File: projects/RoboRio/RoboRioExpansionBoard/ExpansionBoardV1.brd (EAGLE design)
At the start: 100.3 x 80.3 mm, 83 parts, among them Q1 5MHz

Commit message: Deleted some capacitors
just for lol s♥♥♥♥♥♥♥♥
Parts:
- removed C1, C11, C6, C7, C8, C9: (no value), capacitor-wima:C7.5B6
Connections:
- net +3V3: no longer C1.1, C11.2, C6.1, C9.2
- net +5V: no longer C7.1, C8.1
- net GND: no longer C1.2, C11.1, C6.2, C7.2, C8.2, C9.1
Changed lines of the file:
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@@
 <element name="GREEN" library="led" package="LED5MM" value="" x="-91.44" y="-19.05"/>
 <element name="U$4" library="RESETBUTTON3000" package="RESETBUTTON300000MILLION" value="BUTTON" x="89.916" y="74.168" rot="R180"/>
-<element name="C1" library="capacitor-wima" package="C7.5B6" value="" x="-90.17" y="-27.432"/>
 <element name="C4" library="capacitor-wima" package="C7.5B6" value="" x="-90.17" y="-51.816"/>
 <element name="C5" library="capacitor-wima" package="C7.5B6" value="" x="-90.17" y="-59.944"/>
-<element name="C6" library="capacitor-wima" package="C7.5B6" value="" x="-90.17" y="-68.072"/>
-<element name="C7" library="capacitor-wima" package="C7.5B6" value="" x="-90.17" y="-76.2"/>
 <element name="C2" library="capacitor-wima" package="C7.5B6" value="" x="-90.17" y="-84.328"/>
-<element name="C8" library="capacitor-wima" package="C7.5B6" value="" x="-90.17" y="-100.584"/>
 <element name="C3" library="capacitor-wima" package="C7.5B6" value="" x="-90.17" y="-108.712"/>
-<element name="C9" library="capacitor-wima" package="C7.5B6" value="" x="-90.17" y="-116.84"/>
 <element name="C10" library="capacitor-wima" package="C7.5B6" value="" x="-90.17" y="-124.968"/>
-<element name="C11" library="capacitor-wima" package="C7.5B6" value="" x="-90.17" y="-133.096"/>
 <element name="C12" library="capacitor-wima" package="C7.5B6" value="" x="-90.17" y="-141.224"/>
 <element name="C13" library="capacitor-wima" package="C7.5B6" value="" x="-90.17" y="-149.352"/>
@@
 <contactref element="U$4" pad="P4"/>
 <contactref element="U$4" pad="P3"/>
-<contactref element="C1" pad="2"/>
 <contactref element="C4" pad="2"/>
 <contactref element="C5" pad="1"/>
-<contactref element="C6" pad="2"/>
 <contactref element="C2" pad="2"/>
-<contactref element="C8" pad="2"/>
-<contactref element="C7" pad="2"/>
 <contactref element="C3" pad="2"/>
-<contactref element="C9" pad="1"/>
 <contactref element="C10" pad="2"/>
-<contactref element="C11" pad="1"/>
 <contactref element="C12" pad="2"/>
 <contactref element="GREEN1" pad="K"/>
 <wire x1="-86.36" y1="-141.224" x2="-90.932" y2="-155.956" width="0" layer="19" extent="1-1"/>
-<wire x1="-93.98" y1="-133.096" x2="-86.36" y2="-141.224" width="0" layer="19" extent="1-1"/>
-<wire x1="-86.36" y1="-124.968" x2="-93.98" y2="-133.096" width="0" layer="19" extent="1-1"/>
-<wire x1="-93.98" y1="-116.84" x2="-86.36" y2="-124.968" width="0" layer="19" extent="1-1"/>
-<wire x1="-86.36" y1="-108.712" x2="-93.98" y2="-116.84" width="0" layer="19" extent="1-1"/>
-<wire x1="-86.36" y1="-100.584" x2="-86.36" y2="-108.712" width="0" layer="19" extent="1-1"/>
-<wire x1="-86.36" y1="-84.328" x2="-86.36" y2="-100.584" width="0" layer="19" extent="1-1"/>
-<wire x1="-86.36" y1="-76.2" x2="-86.36" y2="-84.328" width="0" layer="19" extent="1-1"/>
-<wire x1="-86.36" y1="-68.072" x2="-86.36" y2="-76.2" width="0" layer="19" extent="1-1"/>
-<wire x1="-93.98" y1="-59.944" x2="-86.36" y2="-68.072" width="0" layer="19" extent="1-1"/>
+<wire x1="-86.36" y1="-124.968" x2="-86.36" y2="-141.224" width="0" layer="19" extent="1-1"/>
+<wire x1="-86.36" y1="-108.712" x2="-86.36" y2="-124.968" width="0" layer="19" extent="1-1"/>
+<wire x1="-86.36" y1="-84.328" x2="-86.36" y2="-108.712" width="0" layer="19" extent="1-1"/>
+<wire x1="-93.98" y1="-59.944" x2="-86.36" y2="-84.328" width="0" layer="19" extent="1-1"/>
 <wire x1="-86.36" y1="-51.816" x2="-93.98" y2="-59.944" width="0" layer="19" extent="1-1"/>
-<wire x1="-86.36" y1="-27.432" x2="-86.36" y2="-51.816" width="0" layer="19" extent="1-1"/>
-<wire x1="-90.17" y1="-19.05" x2="-86.36" y2="-27.432" width="0" layer="19" extent="1-1"/>
+<wire x1="-90.17" y1="-19.05" x2="-86.36" y2="-51.816" width="0" layer="19" extent="1-1"/>
 <wire x1="-90.17" y1="-11.43" x2="-90.17" y2="-19.05" width="0" layer="19" extent="1-1"/>
 <wire x1="-90.17" y1="-3.81" x2="-90.17" y2="-11.43" width="0" layer="19" extent="1-1"/>
@@
 <contactref element="IO30" pad="2"/>
 <contactref element="IO31" pad="2"/>
-<contactref element="C1" pad="1"/>
 <contactref element="C4" pad="1"/>
 <contactref element="C5" pad="2"/>
 <contactref element="C2" pad="1"/>
-<contactref element="C6" pad="1"/>
-<contactref element="C9" pad="2"/>
-<contactref element="C11" pad="2"/>
 <contactref element="C12" pad="1"/>
 <contactref element="GREEN1" pad="A"/>
 <wire x1="-93.98" y1="-141.224" x2="-93.472" y2="-155.956" width="0" layer="19" extent="1-1"/>
-<wire x1="-86.36" y1="-133.096" x2="-93.98" y2="-141.224" width="0" layer="19" extent="1-1"/>
-<wire x1="-86.36" y1="-116.84" x2="-86.36" y2="-133.096" width="0" layer="19" extent="1-1"/>
-<wire x1="-93.98" y1="-84.328" x2="-86.36" y2="-116.84" width="0" layer="19" extent="1-1"/>
-<wire x1="-93.98" y1="-68.072" x2="-93.98" y2="-84.328" width="0" layer="19" extent="1-1"/>
-<wire x1="-86.36" y1="-59.944" x2="-93.98" y2="-68.072" width="0" layer="19" extent="1-1"/>
+<wire x1="-93.98" y1="-84.328" x2="-93.98" y2="-141.224" width="0" layer="19" extent="1-1"/>
+<wire x1="-86.36" y1="-59.944" x2="-93.98" y2="-84.328" width="0" layer="19" extent="1-1"/>
 <wire x1="-93.98" y1="-51.816" x2="-86.36" y2="-59.944" width="0" layer="19" extent="1-1"/>
-<wire x1="-93.98" y1="-27.432" x2="-93.98" y2="-51.816" width="0" layer="19" extent="1-1"/>
-<wire x1="-91.44" y1="10.16" x2="-93.98" y2="-27.432" width="0" layer="19" extent="1-1"/>
+<wire x1="-91.44" y1="10.16" x2="-93.98" y2="-51.816" width="0" layer="19" extent="1-1"/>
 <wire x1="-52.07" y1="2.54" x2="-91.44" y2="10.16" width="0" layer="19" extent="1-1"/>
 <wire x1="-49.53" y1="2.54" x2="-52.07" y2="2.54" width="0" layer="19" extent="1-1"/>
@@
 <contactref element="ADC" pad="15"/>
 <contactref element="5V_LCD" pad="2"/>
-<contactref element="C8" pad="1"/>
-<contactref element="C7" pad="1"/>
 <contactref element="C3" pad="1"/>
 <contactref element="C10" pad="1"/>
@@
 <wire x1="-93.98" y1="-124.968" x2="-93.98" y2="-149.352" width="0" layer="19" extent="1-1"/>
 <wire x1="-93.98" y1="-108.712" x2="-93.98" y2="-124.968" width="0" layer="19" extent="1-1"/>
-<wire x1="-93.98" y1="-100.584" x2="-93.98" y2="-108.712" width="0" layer="19" extent="1-1"/>
-<wire x1="-93.98" y1="-76.2" x2="-93.98" y2="-100.584" width="0" layer="19" extent="1-1"/>
-<wire x1="-88.9" y1="10.16" x2="-93.98" y2="-76.2" width="0" layer="19" extent="1-1"/>
+<wire x1="-88.9" y1="10.16" x2="-93.98" y2="-108.712" width="0" layer="19" extent="1-1"/>
 <wire x1="-52.07" y1="10.16" x2="-88.9" y2="10.16" width="0" layer="19" extent="1-1"/>
 <wire x1="-83.82" y1="83.82" x2="-88.9" y2="10.16" width="0" layer="19" extent="1-1"/>

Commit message: changes
change is coming
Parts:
- added R5: 10k, resistor:0309V
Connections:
- new net N$17: GREEN1.A, R5.1
- net +3V3: now also R5.2; no longer GREEN1.A
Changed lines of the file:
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@@
 <element name="C13" library="capacitor-wima" package="C7.5B6" value="" x="-90.17" y="-149.352"/>
 <element name="GREEN1" library="led" package="LED5MM" value="" x="-92.202" y="-155.956"/>
+<element name="R5" library="resistor" package="0309V" value="10k" x="-92.71" y="-162.052"/>
 </elements>
 <signals>
@@
 <contactref element="C2" pad="1"/>
 <contactref element="C12" pad="1"/>
-<contactref element="GREEN1" pad="A"/>
-<wire x1="-93.98" y1="-141.224" x2="-93.472" y2="-155.956" width="0" layer="19" extent="1-1"/>
+<contactref element="R5" pad="2"/>
+<wire x1="-93.98" y1="-141.224" x2="-91.44" y2="-162.052" width="0" layer="19" extent="1-1"/>
 <wire x1="-93.98" y1="-84.328" x2="-93.98" y2="-141.224" width="0" layer="19" extent="1-1"/>
 <wire x1="-86.36" y1="-59.944" x2="-93.98" y2="-84.328" width="0" layer="19" extent="1-1"/>
@@
 <contactref element="C13" pad="2"/>
 </signal>
+<signal name="N$17">
+<contactref element="GREEN1" pad="A"/>
+<contactref element="R5" pad="1"/>
+<wire x1="-93.98" y1="-162.052" x2="-93.472" y2="-155.956" width="0" layer="19" extent="1-1"/>
+</signal>
 </signals>

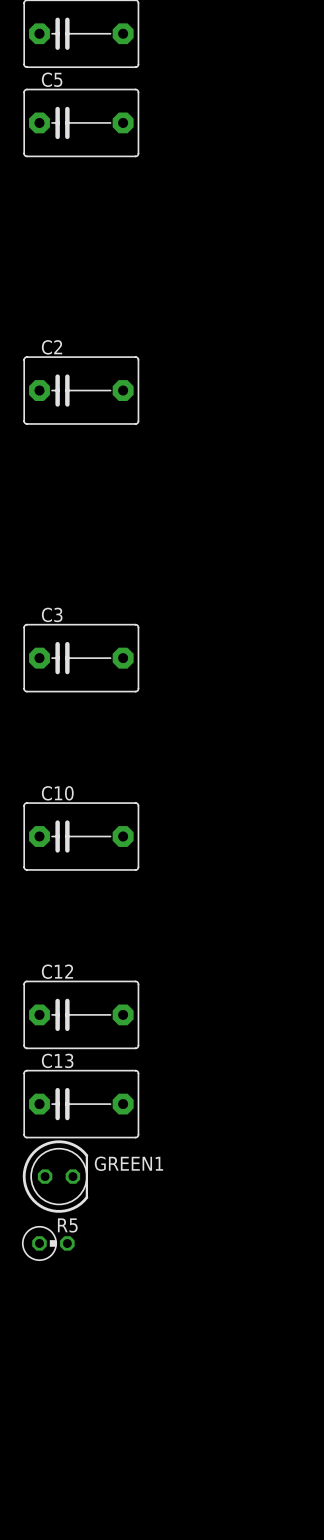
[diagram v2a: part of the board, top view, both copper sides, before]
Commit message: AIO has been broken out
-Eric
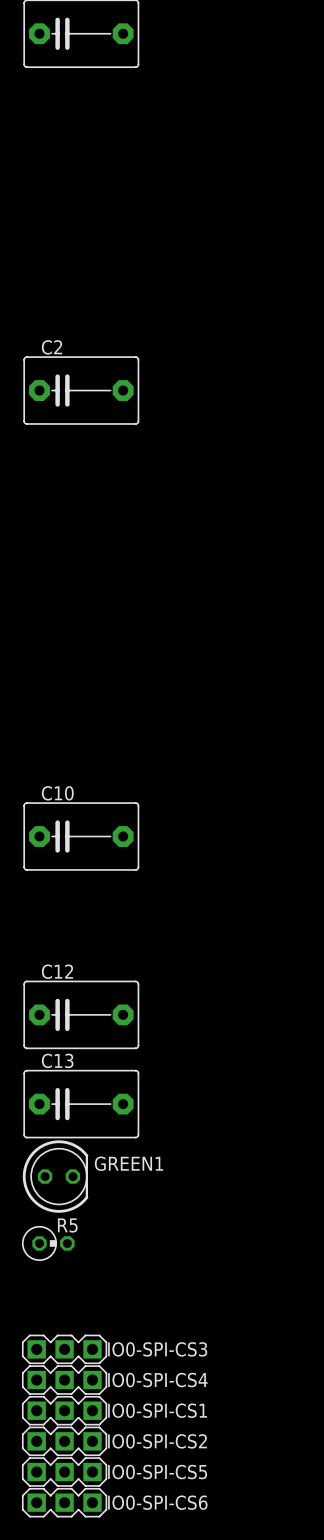
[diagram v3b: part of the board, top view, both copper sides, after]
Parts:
- removed C3, C5: (no value), capacitor-wima:C7.5B6
- added IO0-SPI-CS1, IO0-SPI-CS2, IO0-SPI-CS3, IO0-SPI-CS4, IO0-SPI-CS5, IO0-SPI-CS6: (no value), con-lstb-modified:MA03-1
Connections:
- new net N$18: IO0-SPI-CS1.2, IO0-SPI-CS2.2, IO0-SPI-CS3.2, IO0-SPI-CS4.2, IO0-SPI-CS5.2, IO0-SPI-CS6.2
- net +3V3: no longer C5.2
- net +5V: no longer C3.1
- net AI0: now also IO0-SPI-CS6.3
- net AI1: now also IO0-SPI-CS1.3
- net AI2: now also IO0-SPI-CS3.3
- net AI3: now also IO0-SPI-CS4.3
- net AO0: now also IO0-SPI-CS2.3
- net AO1: now also IO0-SPI-CS5.3
- net GND: now also IO0-SPI-CS1.1, IO0-SPI-CS2.1, IO0-SPI-CS3.1, IO0-SPI-CS4.1, IO0-SPI-CS5.1, IO0-SPI-CS6.1; no longer C3.2, C5.1

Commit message: Added some connections to the ADC
-eric
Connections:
- net IO12: now also ADC.10
- net IO13: now also ADC.11
- net IO14: now also ADC.12
- net IO15: now also ADC.13
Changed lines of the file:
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@@
 <contactref element="PROPELLER" pad="17"/>
 <contactref element="IO12" pad="3"/>
-<wire x1="-66.04" y1="102.87" x2="67.31" y2="17.145" width="0" layer="19" extent="1-1"/>
+<contactref element="ADC" pad="10"/>
+<wire x1="-76.2" y1="10.16" x2="67.31" y2="17.145" width="0" layer="19" extent="1-1"/>
+<wire x1="-66.04" y1="102.87" x2="-76.2" y2="10.16" width="0" layer="19" extent="1-1"/>
 </signal>
 <signal name="IO13">
 <contactref element="PROPELLER" pad="18"/>
 <contactref element="IO13" pad="3"/>
-<wire x1="-76.2" y1="102.87" x2="67.31" y2="14.605" width="0" layer="19" extent="1-1"/>
+<contactref element="ADC" pad="11"/>
+<wire x1="-78.74" y1="10.16" x2="67.31" y2="14.605" width="0" layer="19" extent="1-1"/>
+<wire x1="-76.2" y1="102.87" x2="-78.74" y2="10.16" width="0" layer="19" extent="1-1"/>
 </signal>
 <signal name="IO15">
 <contactref element="PROPELLER" pad="20"/>
 <contactref element="IO15" pad="3"/>
+<contactref element="ADC" pad="13"/>
+<wire x1="-83.82" y1="10.16" x2="-15.24" y2="109.22" width="0" layer="19" extent="1-1"/>
 <wire x1="67.31" y1="9.525" x2="-15.24" y2="109.22" width="0" layer="19" extent="1-1"/>
 </signal>
@@
 <contactref element="PROPELLER" pad="19"/>
 <contactref element="IO14" pad="3"/>
-<wire x1="-86.36" y1="102.87" x2="67.31" y2="12.065" width="0" layer="19" extent="1-1"/>
+<contactref element="ADC" pad="12"/>
+<wire x1="-81.28" y1="10.16" x2="67.31" y2="12.065" width="0" layer="19" extent="1-1"/>
+<wire x1="-86.36" y1="102.87" x2="-81.28" y2="10.16" width="0" layer="19" extent="1-1"/>
 </signal>
 <signal name="N$5">

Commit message: Moved the PWM breakouts
to show its only connected to the roborio,
eric
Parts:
- renumbered IO0-SPI-CS1 to AI1, IO0-SPI-CS2 to AI4, IO0-SPI-CS3 to AI2, IO0-SPI-CS4 to AI3, IO0-SPI-CS5 to AI5, IO0-SPI-CS6 to AIO, RRDIO0 to PWM0, RRDIO1 to PWM1, RRDIO10 to PWM6, RRDIO11 to PWM7, RRDIO12 to PWM8, RRDIO13 to PWM9, RRDIO2 to PWM2, RRDIO3 to PWM3, RRDIO8 to PWM4, RRDIO9 to PWM5

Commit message: Made connections prettier
to better understand it.
eric
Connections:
- net +5V: no longer 5V_LCD.2
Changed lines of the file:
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@@
 <contactref element="IO20" pad="1"/>
 <contactref element="3V3_LCD" pad="1"/>
-<contactref element="5V_LCD" pad="1"/>
 <contactref element="IO17" pad="1"/>
 <contactref element="IO18" pad="1"/>
@@
 <contactref element="AI3" pad="1"/>
 <contactref element="AI4" pad="1"/>
+<contactref element="5V_LCD" pad="1"/>
 <wire x1="-86.36" y1="-141.224" x2="-90.932" y2="-155.956" width="0" layer="19" extent="1-1"/>
 <wire x1="-94.234" y1="-171.704" x2="-90.932" y2="-155.956" width="0" layer="19" extent="1-1"/>
@@
 <contactref element="ADC0" pad="2"/>
 <contactref element="ADC" pad="15"/>
-<contactref element="5V_LCD" pad="2"/>
 <contactref element="C10" pad="1"/>
 <contactref element="C13" pad="1"/>
@@
 <wire x1="-88.9" y1="90.17" x2="-83.82" y2="83.82" width="0" layer="19" extent="1-1"/>
 <wire x1="-68.58" y1="90.17" x2="-78.74" y2="90.17" width="0" layer="19" extent="1-1"/>
-<wire x1="-58.42" y1="90.17" x2="-68.58" y2="90.17" width="0" layer="19" extent="1-1"/>
-<wire x1="-48.26" y1="90.17" x2="-58.42" y2="90.17" width="0" layer="19" extent="1-1"/>
+<wire x1="-48.26" y1="90.17" x2="-68.58" y2="90.17" width="0" layer="19" extent="1-1"/>
 <wire x1="-27.94" y1="90.17" x2="-48.26" y2="90.17" width="0" layer="19" extent="1-1"/>
 <wire x1="-17.78" y1="90.17" x2="-27.94" y2="90.17" width="0" layer="19" extent="1-1"/>

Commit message: Tidied up connections
eric
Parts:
- removed C10: (no value), capacitor-wima:C7.5B6
- added C1: .1uF, capacitor-wima:C7.5B6
- C12: value (none) -> .1 uF
- C13, C2, C4: value (none) -> .1uF
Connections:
- net +3V3: now also C1.2; no longer ADC.16, C4.1
- net +5V: now also 5V_LCD.2, ADC.16, C4.1; no longer C10.1
- net GND: now also C1.1; no longer C10.2
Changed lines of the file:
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@@
 <element name="GREEN" library="led" package="LED5MM" value="" x="-91.44" y="-19.05"/>
 <element name="U$4" library="RESETBUTTON3000" package="RESETBUTTON300000MILLION" value="BUTTON" x="89.916" y="74.168" rot="R180"/>
-<element name="C4" library="capacitor-wima" package="C7.5B6" value="" x="-90.17" y="-51.816"/>
-<element name="C2" library="capacitor-wima" package="C7.5B6" value="" x="-90.17" y="-84.328"/>
-<element name="C10" library="capacitor-wima" package="C7.5B6" value="" x="-90.17" y="-124.968"/>
-<element name="C12" library="capacitor-wima" package="C7.5B6" value="" x="-90.17" y="-141.224"/>
-<element name="C13" library="capacitor-wima" package="C7.5B6" value="" x="-90.17" y="-149.352"/>
+<element name="C4" library="capacitor-wima" package="C7.5B6" value=".1uF" x="-90.17" y="-51.816"/>
+<element name="C2" library="capacitor-wima" package="C7.5B6" value=".1uF" x="-90.17" y="-84.328"/>
+<element name="C12" library="capacitor-wima" package="C7.5B6" value=".1 uF" x="-90.17" y="-141.224"/>
+<element name="C13" library="capacitor-wima" package="C7.5B6" value=".1uF" x="-90.17" y="-149.352"/>
 <element name="GREEN1" library="led" package="LED5MM" value="" x="-92.202" y="-155.956"/>
 <element name="R5" library="resistor" package="0309V" value="10k" x="-92.71" y="-162.052"/>
@@
 <attribute name="OC_FARNELL" value="unknown" x="-91.694" y="-185.674" size="1.778" layer="27" display="off"/>
 </element>
+<element name="C1" library="capacitor-wima" package="C7.5B6" value=".1uF" x="-90.17" y="-192.024"/>
 </elements>
 <signals>
@@
 <contactref element="C4" pad="2"/>
 <contactref element="C2" pad="2"/>
-<contactref element="C10" pad="2"/>
 <contactref element="C12" pad="2"/>
 <contactref element="GREEN1" pad="K"/>
@@
 <contactref element="AI4" pad="1"/>
 <contactref element="5V_LCD" pad="1"/>
+<contactref element="C1" pad="1"/>
 <wire x1="-86.36" y1="-141.224" x2="-90.932" y2="-155.956" width="0" layer="19" extent="1-1"/>
 <wire x1="-94.234" y1="-171.704" x2="-90.932" y2="-155.956" width="0" layer="19" extent="1-1"/>
@@
 <wire x1="-94.234" y1="-182.88" x2="-94.234" y2="-180.086" width="0" layer="19" extent="1-1"/>
 <wire x1="-94.234" y1="-185.674" x2="-94.234" y2="-182.88" width="0" layer="19" extent="1-1"/>
-<wire x1="-86.36" y1="-124.968" x2="-86.36" y2="-141.224" width="0" layer="19" extent="1-1"/>
-<wire x1="-86.36" y1="-84.328" x2="-86.36" y2="-124.968" width="0" layer="19" extent="1-1"/>
+<wire x1="-93.98" y1="-192.024" x2="-94.234" y2="-185.674" width="0" layer="19" extent="1-1"/>
+<wire x1="-86.36" y1="-84.328" x2="-86.36" y2="-141.224" width="0" layer="19" extent="1-1"/>
 <wire x1="-86.36" y1="-51.816" x2="-86.36" y2="-84.328" width="0" layer="19" extent="1-1"/>
 <wire x1="-90.17" y1="-19.05" x2="-86.36" y2="-51.816" width="0" layer="19" extent="1-1"/>
@@
 <contactref element="PROPELLER" pad="32"/>
 <contactref element="PROPELLER" pad="12"/>
-<contactref element="ADC" pad="16"/>
 <contactref element="LEVELSHIFTER" pad="1"/>
 <contactref element="LEVELSHIFTER" pad="2"/>
@@
 <contactref element="IO30" pad="2"/>
 <contactref element="IO31" pad="2"/>
-<contactref element="C4" pad="1"/>
 <contactref element="C2" pad="1"/>
 <contactref element="C12" pad="1"/>
 <contactref element="R5" pad="2"/>
+<contactref element="C1" pad="2"/>
 <wire x1="-93.98" y1="-141.224" x2="-91.44" y2="-162.052" width="0" layer="19" extent="1-1"/>
+<wire x1="-86.36" y1="-192.024" x2="-91.44" y2="-162.052" width="0" layer="19" extent="1-1"/>
 <wire x1="-93.98" y1="-84.328" x2="-93.98" y2="-141.224" width="0" layer="19" extent="1-1"/>
-<wire x1="-93.98" y1="-51.816" x2="-93.98" y2="-84.328" width="0" layer="19" extent="1-1"/>
-<wire x1="-91.44" y1="10.16" x2="-93.98" y2="-51.816" width="0" layer="19" extent="1-1"/>
-<wire x1="-52.07" y1="2.54" x2="-91.44" y2="10.16" width="0" layer="19" extent="1-1"/>
+<wire x1="-52.07" y1="2.54" x2="-93.98" y2="-84.328" width="0" layer="19" extent="1-1"/>
 <wire x1="-49.53" y1="2.54" x2="-52.07" y2="2.54" width="0" layer="19" extent="1-1"/>
 <wire x1="-36.83" y1="2.54" x2="-49.53" y2="2.54" width="0" layer="19" extent="1-1"/>
-<wire x1="-68.58" y1="73.66" x2="-91.44" y2="10.16" width="0" layer="19" extent="1-1"/>
+<wire x1="-68.58" y1="73.66" x2="-52.07" y2="2.54" width="0" layer="19" extent="1-1"/>
 <wire x1="-62.23" y1="83.82" x2="-68.58" y2="73.66" width="0" layer="19" extent="1-1"/>
 <wire x1="-49.53" y1="83.82" x2="-62.23" y2="83.82" width="0" layer="19" extent="1-1"/>
@@
 <contactref element="ADC1" pad="2"/>
 <contactref element="ADC0" pad="2"/>
+<contactref element="C13" pad="1"/>
+<contactref element="5V_LCD" pad="2"/>
+<contactref element="ADC" pad="16"/>
+<contactref element="C4" pad="1"/>
 <contactref element="ADC" pad="15"/>
-<contactref element="C10" pad="1"/>
-<contactref element="C13" pad="1"/>
-<wire x1="-93.98" y1="-124.968" x2="-93.98" y2="-149.352" width="0" layer="19" extent="1-1"/>
-<wire x1="-88.9" y1="10.16" x2="-93.98" y2="-124.968" width="0" layer="19" extent="1-1"/>
+<wire x1="-93.98" y1="-51.816" x2="-93.98" y2="-149.352" width="0" layer="19" extent="1-1"/>
+<wire x1="-91.44" y1="10.16" x2="-93.98" y2="-51.816" width="0" layer="19" extent="1-1"/>
+<wire x1="-88.9" y1="10.16" x2="-91.44" y2="10.16" width="0" layer="19" extent="1-1"/>
 <wire x1="-52.07" y1="10.16" x2="-88.9" y2="10.16" width="0" layer="19" extent="1-1"/>
 <wire x1="-83.82" y1="83.82" x2="-88.9" y2="10.16" width="0" layer="19" extent="1-1"/>
@@
 <wire x1="-88.9" y1="90.17" x2="-83.82" y2="83.82" width="0" layer="19" extent="1-1"/>
 <wire x1="-68.58" y1="90.17" x2="-78.74" y2="90.17" width="0" layer="19" extent="1-1"/>
-<wire x1="-48.26" y1="90.17" x2="-68.58" y2="90.17" width="0" layer="19" extent="1-1"/>
+<wire x1="-58.42" y1="90.17" x2="-68.58" y2="90.17" width="0" layer="19" extent="1-1"/>
+<wire x1="-48.26" y1="90.17" x2="-58.42" y2="90.17" width="0" layer="19" extent="1-1"/>
 <wire x1="-27.94" y1="90.17" x2="-48.26" y2="90.17" width="0" layer="19" extent="1-1"/>
 <wire x1="-17.78" y1="90.17" x2="-27.94" y2="90.17" width="0" layer="19" extent="1-1"/>
